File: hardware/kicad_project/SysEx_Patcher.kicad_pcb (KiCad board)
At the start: 4 copper layers, 212 x 180 mm, 88 parts, among them J1 MIDI_IN, J10 JACK6.35, J2 MIDI_OUT, J3 DC_5V, J4 BAT_PWR, J5 OLED, J6A AN_row0, J6B AN_row1, J6C AN_row2, J6D AN_row3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

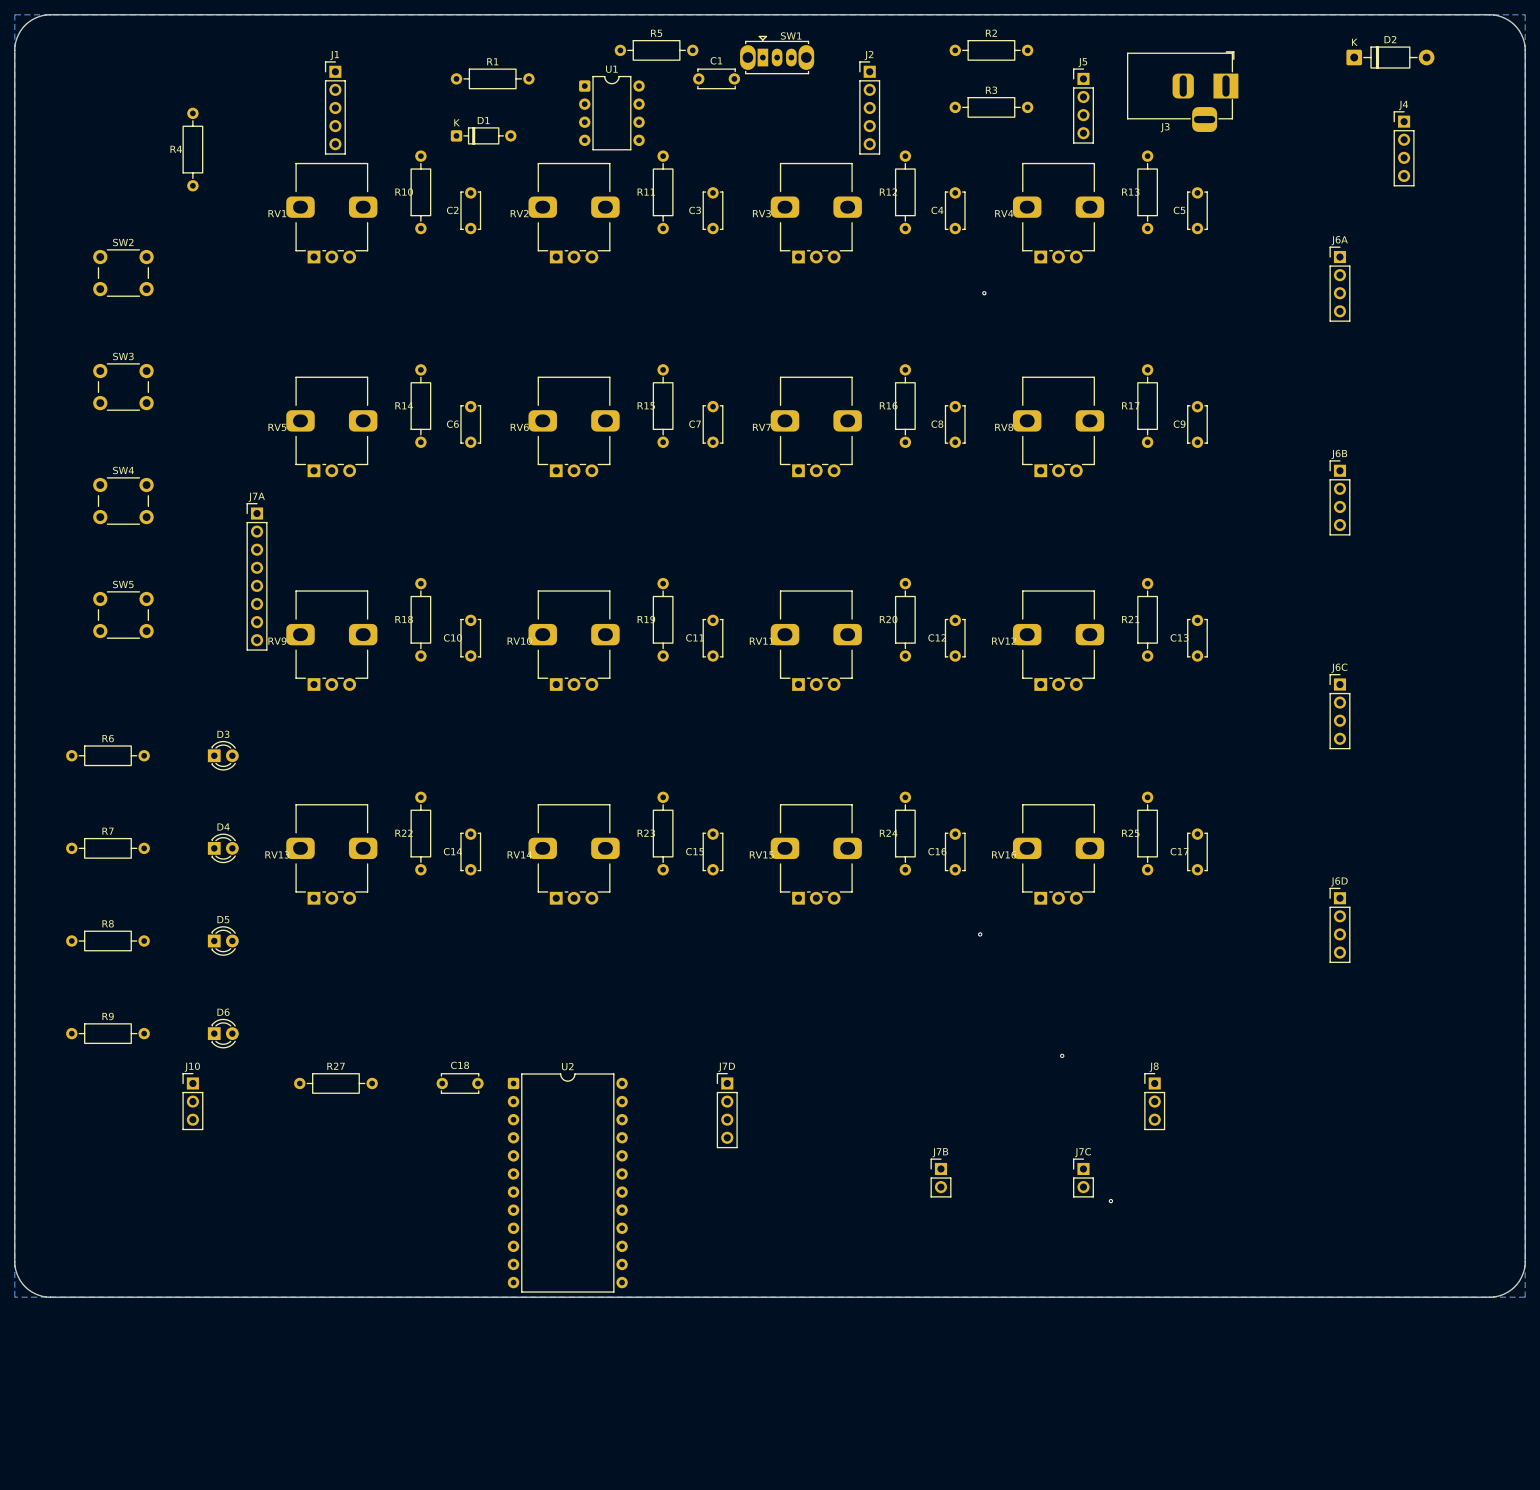
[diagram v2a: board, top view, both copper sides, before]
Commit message: hardware: real pluggable Arduino Mega 2560 shield (THT, fully routed)
Re-laid out as a true stackable shield: Mega connectors at the exact Arduino
Mega 2560 header positions (two rows 48.26mm apart, pinout derived from the
original copper, analog A0..A15 order verified) so the Mega plugs underneath.
Layout: inputs (MIDI in/out, jack, DC) on top, 16 pots in a 4x4 grid each with
its RC filter alongside, 4 push buttons in a vertical column, LEDs on the right,
Mega header block at the bottom. 100% THT, 4 layers + GND plane, fully routed
(0 unconnected), DRC clean (only cosmetic silkscreen), rounded corners ~172x205mm.
Mux 4th select moved D22->D13 (D22 not on these two header rows). Gerbers updated.
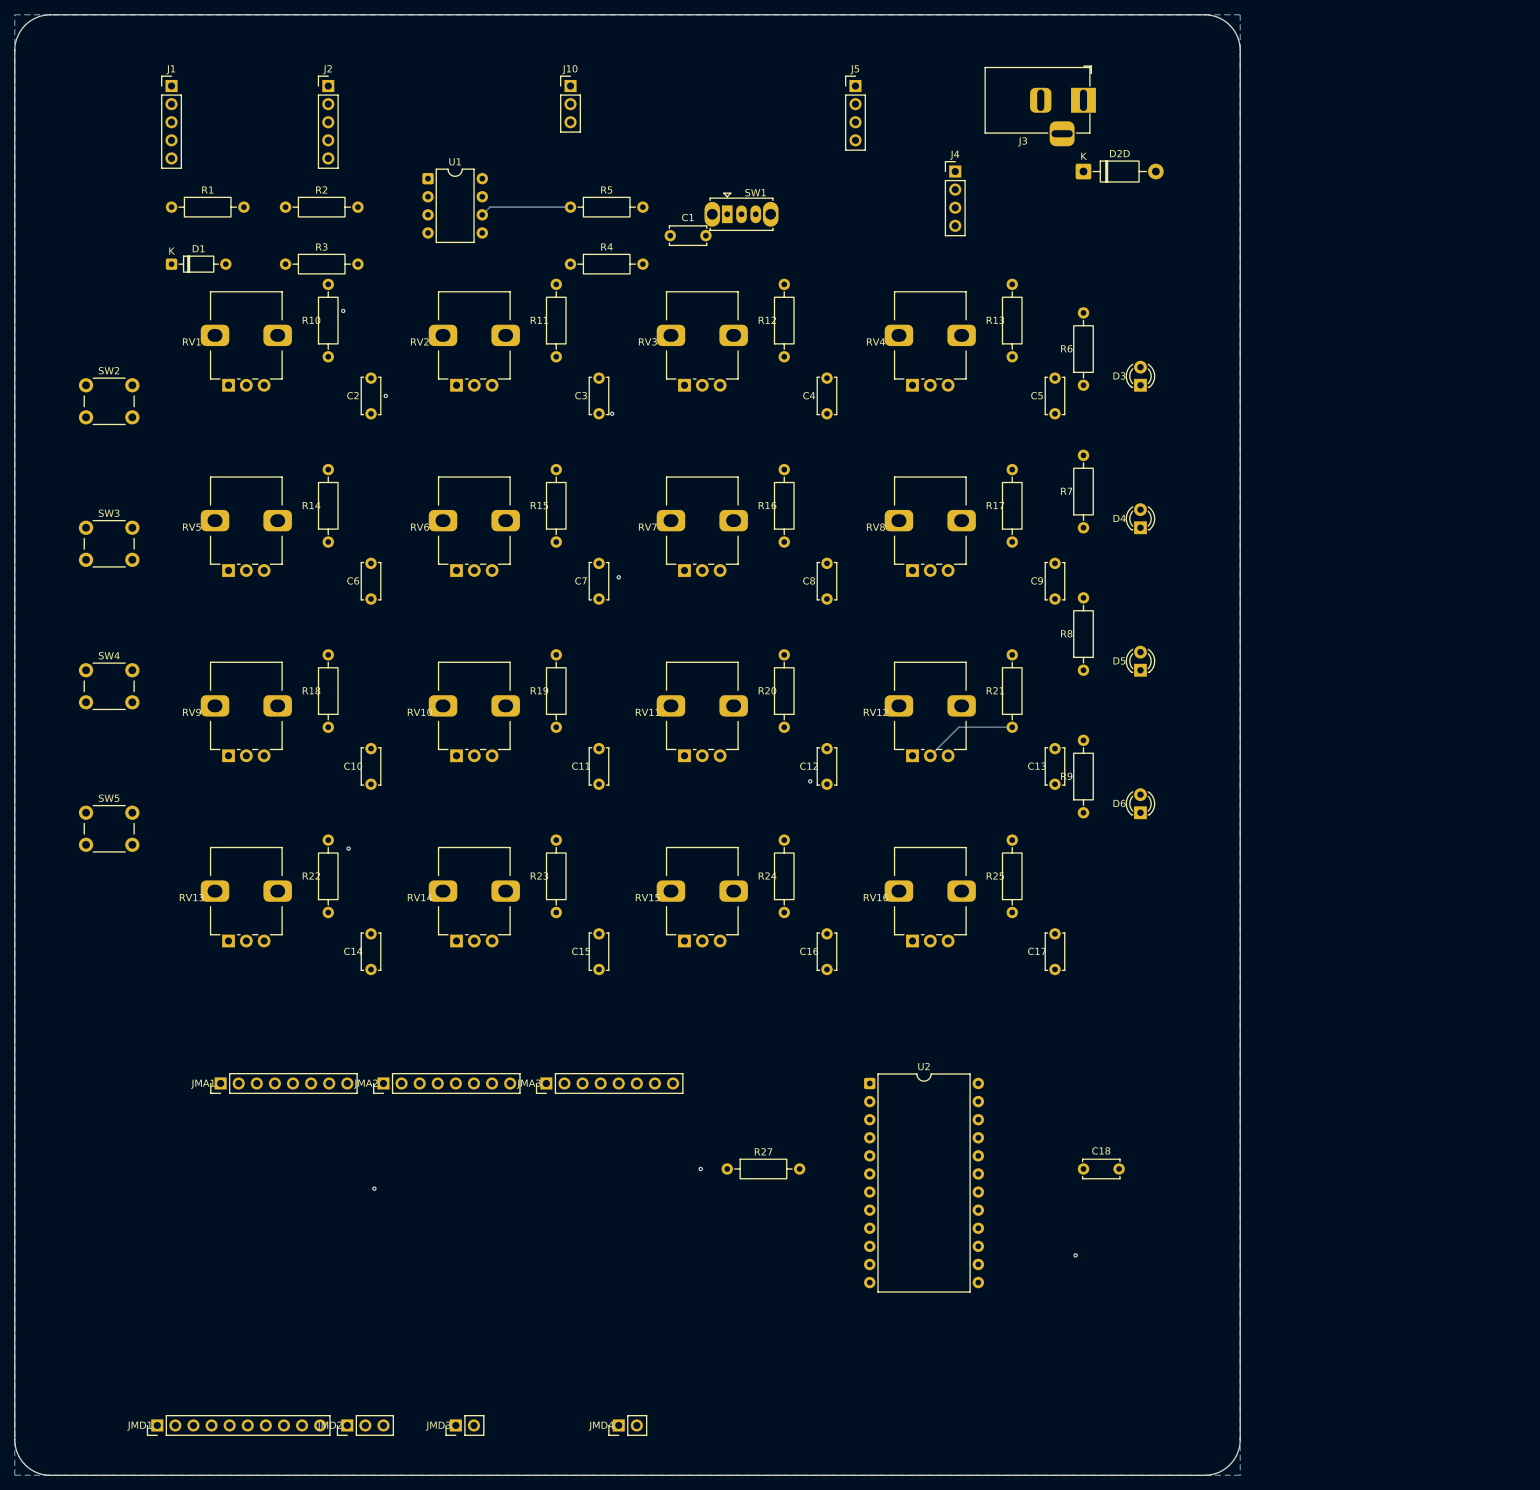
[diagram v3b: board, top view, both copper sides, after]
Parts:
- removed D2: 1N4004, Diode_THT:D_DO-41_SOD81_P10.16mm_Horizontal
- removed J6A: AN_row0, Connector_PinHeader_2.54mm:PinHeader_1x04_P2.54mm_Vertical
- removed J6B: AN_row1, Connector_PinHeader_2.54mm:PinHeader_1x04_P2.54mm_Vertical
- removed J6C: AN_row2, Connector_PinHeader_2.54mm:PinHeader_1x04_P2.54mm_Vertical
- removed J6D: AN_row3, Connector_PinHeader_2.54mm:PinHeader_1x04_P2.54mm_Vertical
- removed J7A: DIG_btnled, Connector_PinHeader_2.54mm:PinHeader_1x08_P2.54mm_Vertical
- removed J7B: DIG_midi, Connector_PinHeader_2.54mm:PinHeader_1x02_P2.54mm_Vertical
- removed J7C: DIG_i2c, Connector_PinHeader_2.54mm:PinHeader_1x02_P2.54mm_Vertical
- removed J7D: DIG_muxsel, Connector_PinHeader_2.54mm:PinHeader_1x04_P2.54mm_Vertical
- removed J8: MEGA_PWR, Connector_PinHeader_2.54mm:PinHeader_1x03_P2.54mm_Vertical
- added D2D: 1N4004, Diode_THT:D_DO-41_SOD81_P10.16mm_Horizontal, F.Cu at (150.0, 22.0)
- added JMA1: MEGA, Connector_PinHeader_2.54mm:PinHeader_1x08_P2.54mm_Vertical, F.Cu at (28.9, 150.0)
- added JMA2: MEGA, Connector_PinHeader_2.54mm:PinHeader_1x08_P2.54mm_Vertical, F.Cu at (51.8, 150.0)
- added JMA3: MEGA, Connector_PinHeader_2.54mm:PinHeader_1x08_P2.54mm_Vertical, F.Cu at (74.6, 150.0)
- added JMD1: MEGA, Connector_PinHeader_2.54mm:PinHeader_1x10_P2.54mm_Vertical, F.Cu at (20.0, 198.0)
- added JMD2: MEGA, Connector_PinHeader_2.54mm:PinHeader_1x03_P2.54mm_Vertical, F.Cu at (46.7, 198.0)
- added JMD3: MEGA, Connector_PinHeader_2.54mm:PinHeader_1x02_P2.54mm_Vertical, F.Cu at (61.9, 198.0)
- added JMD4: MEGA, Connector_PinHeader_2.54mm:PinHeader_1x02_P2.54mm_Vertical, F.Cu at (84.8, 198.0)
- moved R6 151.2 mm to (150.0, 52.0), turned to 90 degrees
- moved J10 149.7 mm to (78.0, 10.0)
- moved R7 149.0 mm to (150.0, 72.0), turned to 90 degrees
- moved R8 147.0 mm to (150.0, 92.0), turned to 90 degrees
- moved R9 145.3 mm to (150.0, 112.0), turned to 90 degrees
- moved D3 140.0 mm to (158.0, 52.0), turned to 90 degrees
- moved D4 137.6 mm to (158.0, 72.0), turned to 90 degrees
- moved D5 135.4 mm to (158.0, 92.0), turned to 90 degrees
- moved D6 133.6 mm to (158.0, 112.0), turned to 90 degrees
- moved R2 96.5 mm to (38.0, 27.0)
- moved R3 96.5 mm to (38.0, 35.0)
- moved C18 90.8 mm to (150.0, 162.0)
- moved J2 76.0 mm to (44.0, 10.0)
- moved J4 63.4 mm to (132.0, 22.0)
- moved R27 61.2 mm to (100.0, 162.0)
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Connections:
- U2 pad 13: D22 -> D13
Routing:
- net D12: track 35.9 -> 249.0 mm, vias 0 -> 1
- net D11: track 45.1 -> 203.7 mm, vias 0 -> 1
- net JACK_W: track 15.0 -> 163.5 mm, vias 0 -> 1
- net D10: track 55.5 -> 194.9 mm, vias 0 -> 1
- net A12: track 42.8 -> 162.4 mm, vias 0 -> 1
- net D13: track 0.00 -> 114.7 mm
- net D7: track 48.9 -> 161.3 mm
- net D8: track 35.5 -> 145.8 mm
- net D9: track 66.0 -> 169.2 mm, vias 0 -> 1
- net A3: track 137.6 -> 40.5 mm
- net A15: track 123.6 -> 27.6 mm
- net D4: track 26.4 -> 121.9 mm
- net D6: track 25.8 -> 120.3 mm
- net +5V: track 707.4 -> 622.2 mm, vias 1 -> 0
- net MUX_CH0: track 150.0 -> 68.1 mm, vias 1 -> 0
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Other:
- board size 212 x 180 mm -> 172 x 205 mm

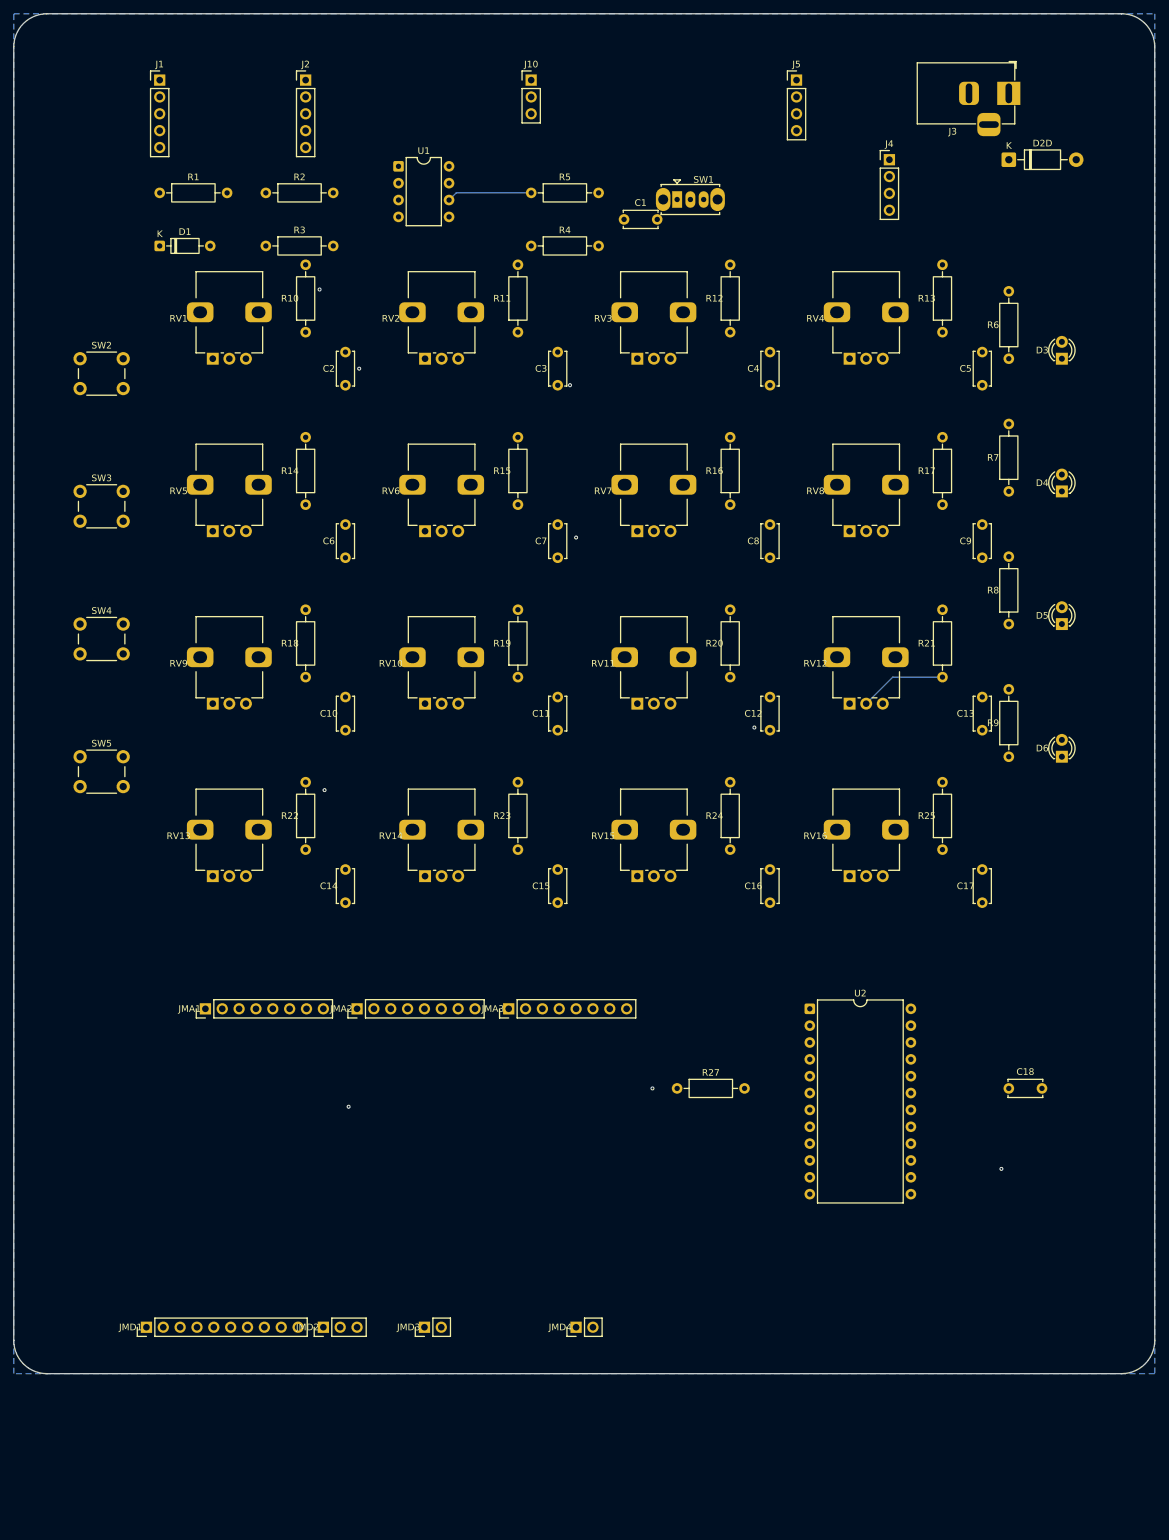
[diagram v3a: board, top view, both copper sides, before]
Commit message: hardware: real MIDI DIN-5 + 6.35mm jack footprints on the shield
Replaced placeholder connectors with proper footprints: custom MIDI DIN-5 180deg
footprint (geometry taken from the original board's drill, vertical) in a project
library, and the vertical Neutrik 6.35mm TRS jack (T/R/S) for the remote-pot jack.
Reorganized the top connector area and re-routed: fully routed (0 unconnected),
DRC clean except 1 trivial track-to-mounting-pad clearance to nudge by hand.
Gerbers updated; added project fp-lib-table + SysEx_Patcher.pretty.
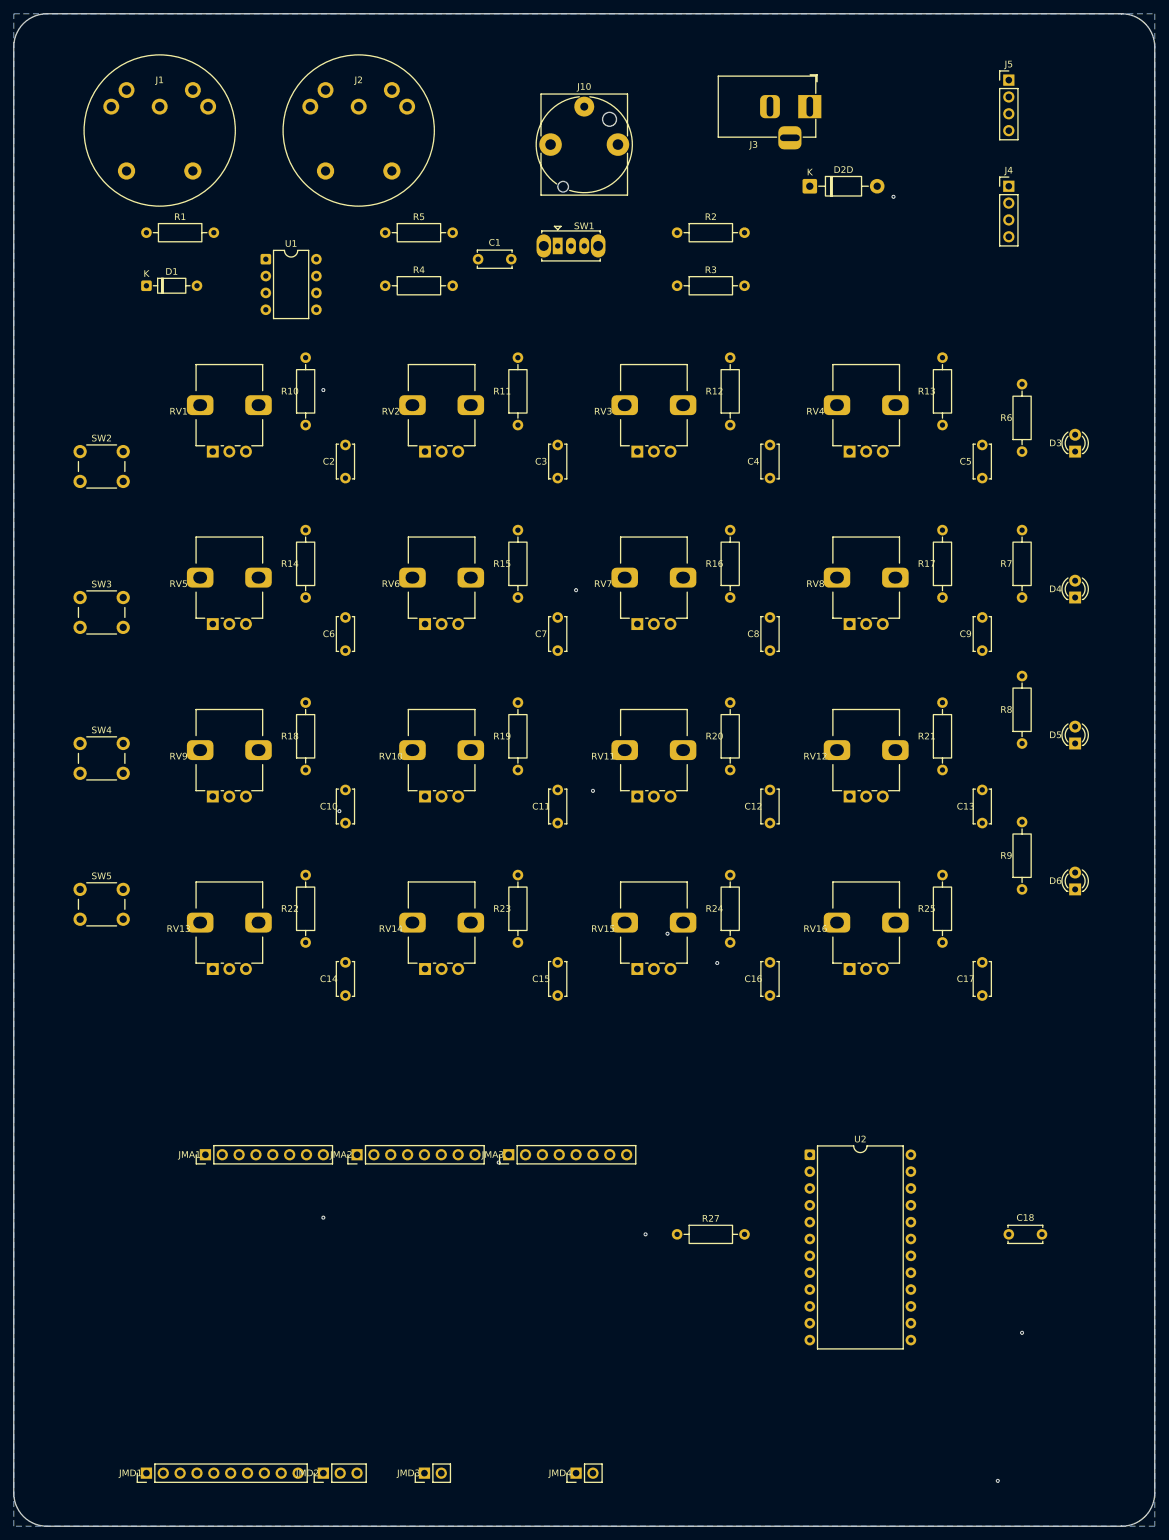
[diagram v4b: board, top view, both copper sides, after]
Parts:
- J1, J2: footprint Connector_PinHeader_2.54mm:PinHeader_1x05_P2.54mm_Vertical -> SysEx_Patcher:MIDI_DIN5_180deg
- J10: footprint Connector_PinHeader_2.54mm:PinHeader_1x03_P2.54mm_Vertical -> Connector_Audio:Jack_6.35mm_Neutrik_NJ3FD-V_Vertical
- moved R2 62.3 mm to (100.0, 33.0)
- moved R3 62.3 mm to (100.0, 41.0)
- moved J5 32.0 mm to (150.0, 10.0)
- moved D2D 30.3 mm to (120.0, 26.0)
- moved J3 30.1 mm to (120.0, 14.0)
- moved U1 24.4 mm to (38.0, 37.0)
- moved C1 22.8 mm to (70.0, 37.0)
- moved R4 22.8 mm to (56.0, 41.0)
- moved R5 22.8 mm to (56.0, 33.0)
- moved C18 22.0 mm to (150.0, 184.0)
- moved JMA1 22.0 mm to (28.9, 172.0)
- moved JMA2 22.0 mm to (51.8, 172.0)
- moved JMA3 22.0 mm to (74.6, 172.0)
- moved JMD1 22.0 mm to (20.0, 220.0)
- moved JMD2 22.0 mm to (46.7, 220.0)
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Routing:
- net +5V: track 622.2 -> 672.4 mm, vias 0 -> 1
- net MIDI_OUT_5: track 17.3 -> 65.2 mm
- net MIDI_OUT_4: track 11.9 -> 51.9 mm
- net D21_SCL: track 195.6 -> 231.9 mm
- net D1_TX: track 168.7 -> 202.6 mm
- net A13: track 113.0 -> 143.0 mm, vias 0 -> 1
- net D20_SDA: track 203.1 -> 229.4 mm
- net D10: track 194.9 -> 176.2 mm
- net D11: track 203.7 -> 221.8 mm
- net D9: track 169.2 -> 186.4 mm
- net OPTO_ANODE: track 41.0 -> 24.0 mm
- net A5: track 122.3 -> 138.7 mm
- net JACK_W: track 163.5 -> 178.6 mm
- net D7: track 161.3 -> 175.8 mm
- net MIDI_IN_4: track 10.4 -> 24.4 mm
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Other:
- board size 172 x 205 mm -> 172 x 228 mm
